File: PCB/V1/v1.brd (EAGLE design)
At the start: 25.1 x 34.3 mm, 1 part

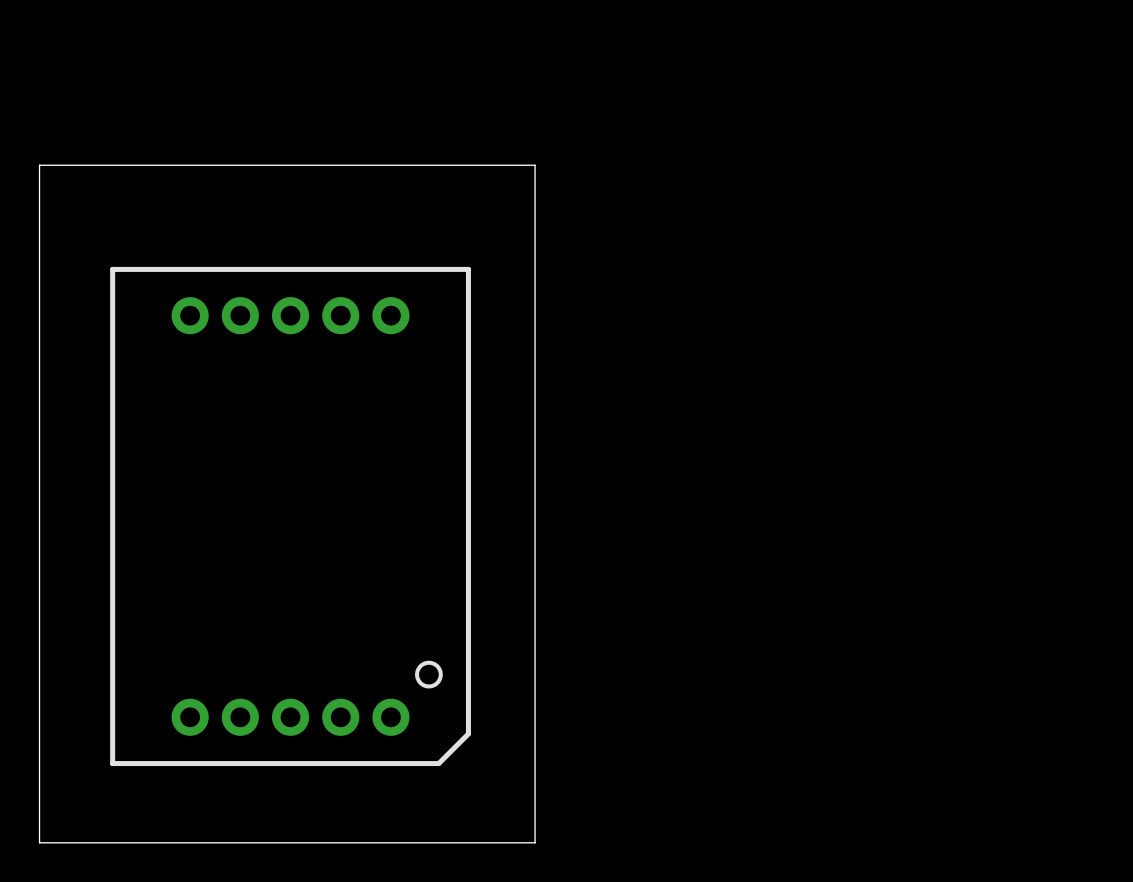
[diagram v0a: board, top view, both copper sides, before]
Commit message: first pcb to test 7 segment, temperature sensor not added yet.
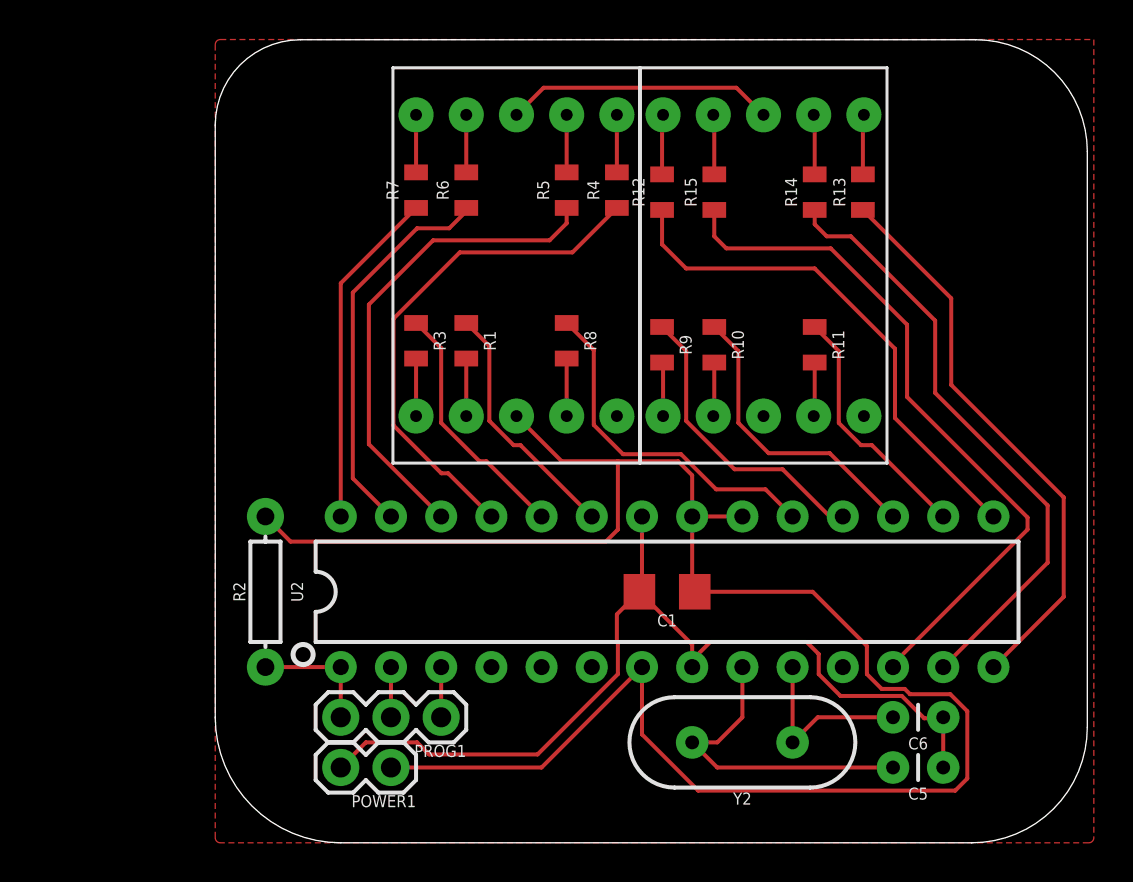
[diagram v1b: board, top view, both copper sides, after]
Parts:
- added C1: 2.2uF, SparkFun-Capacitors:1206
- added C5, C6: 22pF, SparkFun-Capacitors:CAP-PTH-2.54
- added POWER1: (no value), SparkFun-Connectors:1X02
- added PROG1: (no value), SparkFun-Connectors:1X03
- added R1, R10, R11, R12, R13, R14, R15, R3, R4, R5, R6, R7, R8, R9: 10k, SparkFun-Resistors:0805
- added R2: 10k, SparkFun-Resistors:AXIAL-0.3
- added U$2: 7SEGMENTCA, 7segmentca:7SEGMENTCA
- added U2: 328P, SparkFun-IC-Microcontroller:DIP28
- added Y2: 16MHz, SparkFun-Clocks:HC49US
- U$1: value YSD-160AB3C-8 -> 7SEGMENTCA; device SparkFun-LED:7-SEGMENT-1"PTH -> 7segmentca:7SEGMENTCA
- moved U$1 17.1 mm to (24.1, 29.2)
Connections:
- new net 5V: C1.1, POWER1.1, R2.P$2, U$1.A1, U$1.A2, U$2.A1, U$2.A2, U2.20, U2.21, U2.7
- new net GND: C1.2, C5.1, C6.1, POWER1.2, U2.22, U2.8
- new net N$1: C5.2, U2.9, Y2.2
- new net N$10: R6.2, U$1.F
- new net N$11: R5.2, U$1.A
- new net N$12: R4.2, U$1.B
- new net N$13: R3.2, U$1.E
- new net N$14: R1.2, U$1.D
- new net N$15: R8.1, U2.19
- new net N$16: R8.2, U$1.C
- new net N$17: R12.1, U2.15
- new net N$18: R11.1, U2.16
- new net N$19: R10.1, U2.17
- new net N$2: C6.2, U2.10, Y2.1
- new net N$20: R9.1, U2.18
- new net N$21: R9.2, U$2.E
- new net N$22: R10.2, U$2.D
- new net N$23: R11.2, U$2.C
- new net N$24: R12.2, U$2.G
- new net N$25: R15.1, U2.12
- new net N$26: R14.1, U2.13
- new net N$27: R13.1, U2.14
- new net N$28: R15.2, U$2.F
- new net N$29: R14.2, U$2.A
- new net N$3: R1.1, U2.23
- new net N$30: R13.2, U$2.B
- new net N$4: R3.1, U2.24
- new net N$5: R4.1, U2.25
- new net N$6: R5.1, U2.26
- new net N$7: R6.1, U2.27
- new net N$8: R7.1, U2.28
- new net N$9: R7.2, U$1.G
- new net RESET: PROG1.3, R2.P$1, U2.1
- new net RX: PROG1.1, U2.3
- new net TX: PROG1.2, U2.2
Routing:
- net 5V: track 0.00 -> 110.9 mm
- net GND: track 0.00 -> 48.1 mm
- net N$25: track 0.00 -> 35.6 mm
- net N$26: track 0.00 -> 30.9 mm
- net N$27: track 0.00 -> 28.8 mm
- net N$17: track 0.00 -> 26.3 mm
- net N$5: track 0.00 -> 25.9 mm
- net N$6: track 0.00 -> 24.7 mm
- net N$7: track 0.00 -> 19.7 mm
- net N$15: track 0.00 -> 17.7 mm
- net N$8: track 0.00 -> 17.2 mm
- net N$1: track 0.00 -> 16.3 mm
- net N$20: track 0.00 -> 15.2 mm
- net N$19: track 0.00 -> 15.1 mm
- net N$4: track 0.00 -> 12.6 mm
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- added copper zone on layer 1, net NEW
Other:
- board size 25.1 x 34.3 mm -> 44.1 x 40.6 mm
